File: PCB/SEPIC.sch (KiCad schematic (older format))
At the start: 45 parts, among them Q13 DMN6068LK3-13, Q3 MMBT3904-TP, U12 ZXGD3009E6TA, U13 TS462CDT, U17 LM3481MM

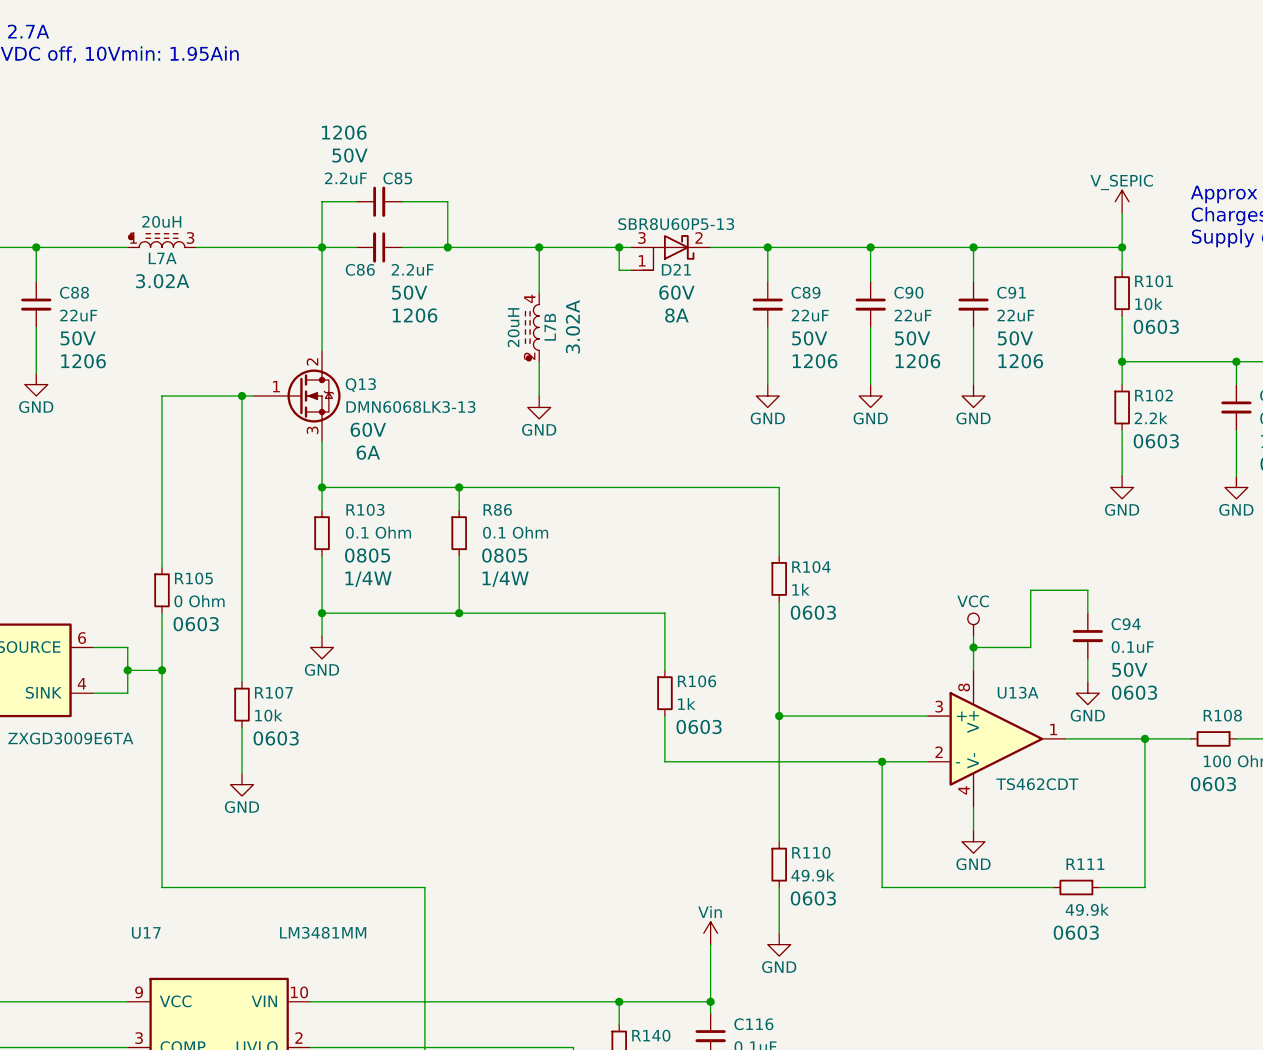
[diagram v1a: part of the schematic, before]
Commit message: Added ELOAD to sch and imported to layout
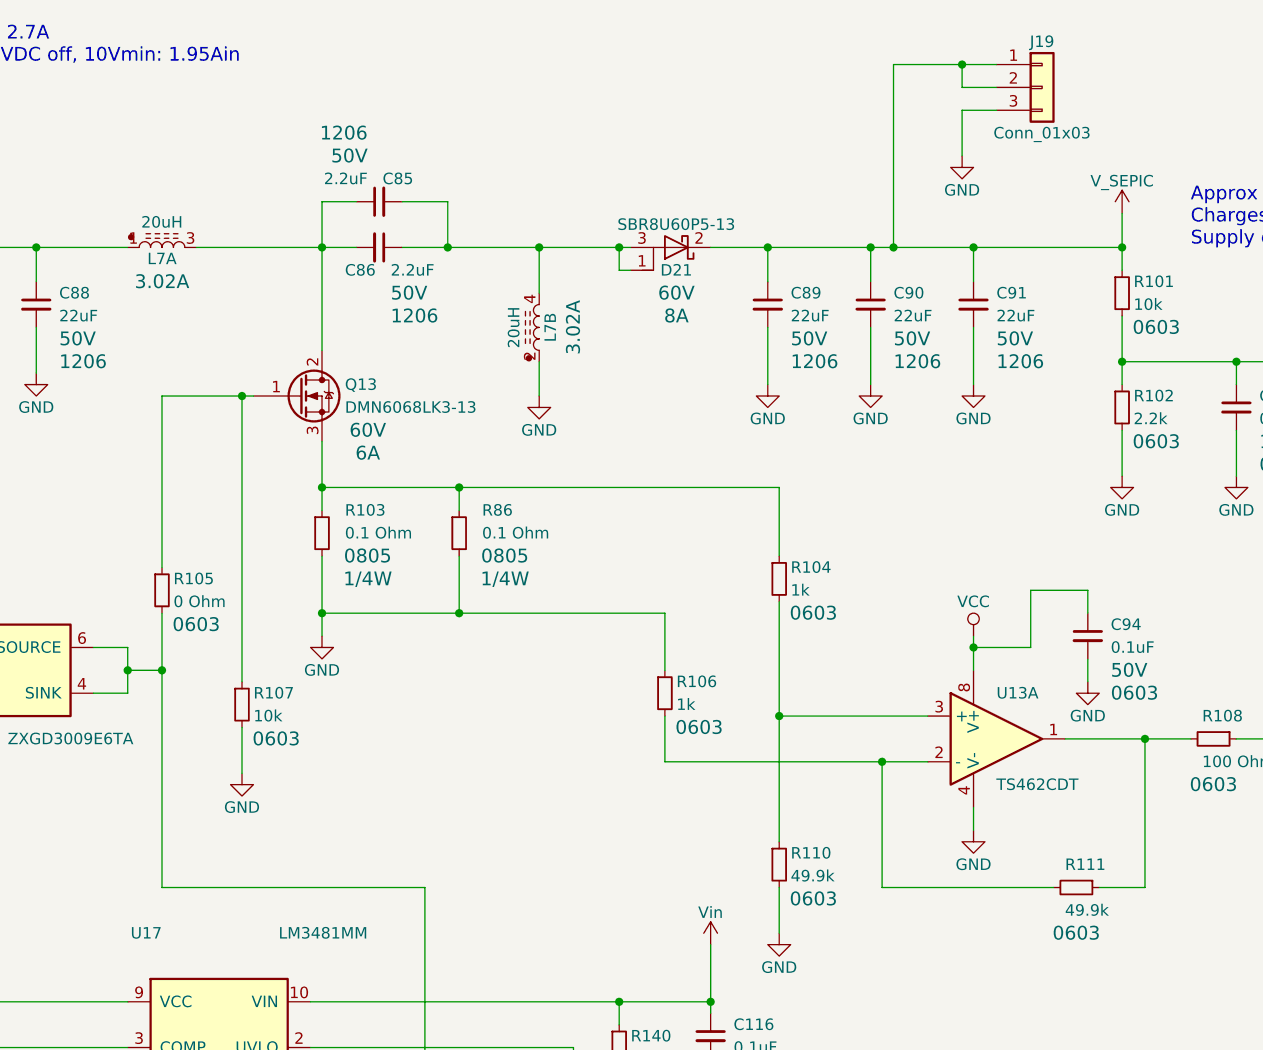
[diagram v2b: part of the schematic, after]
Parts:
- added J19: Conn_01x03, Pin_Headers:Pin_Header_Straight_1x03_Pitch2.54mm_SMD_Pin1Right, symbol Conn_01x03
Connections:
- net GND: now also J19.3 (Pin_3)
- net V_SEPIC: now also J19.1 (Pin_1), J19.2 (Pin_2)
